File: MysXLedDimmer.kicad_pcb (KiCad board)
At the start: 2 copper layers, 18.5 x 26.1 mm, 8 parts, among them P1 MYSX_1.3, P2 CONN_01X02, P3 CONN_01X02, P4 CONN_01X02, Q1 IRLZ44N, Q2 IRLZ44N

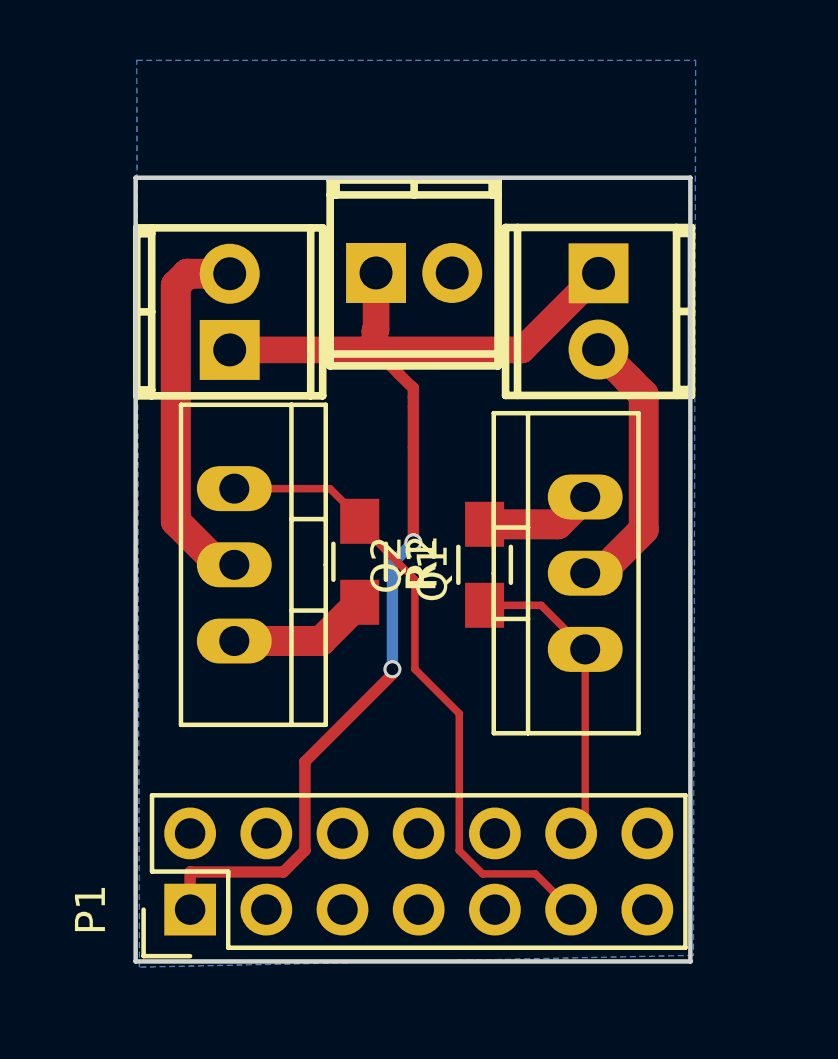
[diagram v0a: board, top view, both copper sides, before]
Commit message: Changed to use IRLML2502 in sot23
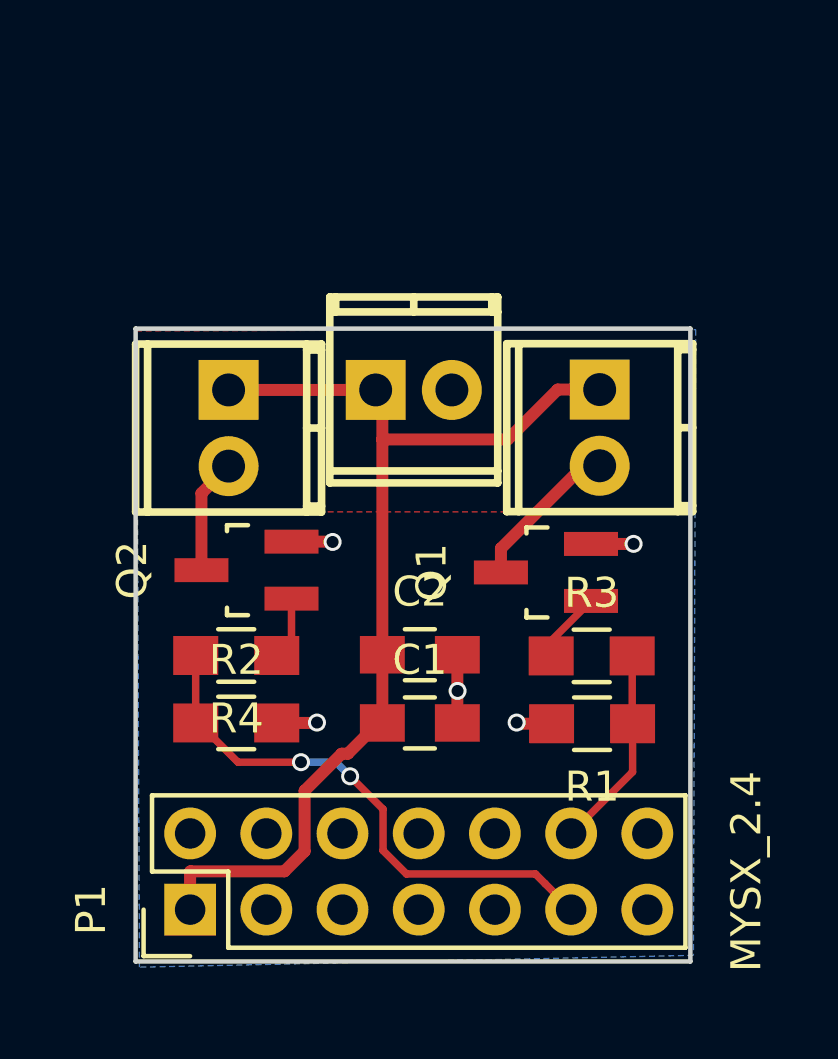
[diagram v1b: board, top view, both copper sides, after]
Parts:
- added C1: C, Capacitors_SMD:C_0805_HandSoldering, F.Cu at (145.5, 118.0)
- added C2: CP, Capacitors_SMD:C_0805_HandSoldering, F.Cu at (145.5, 115.7)
- added R3: 27, Resistors_SMD:R_0805_HandSoldering, F.Cu at (151.2, 115.7)
- added R4: 27, Resistors_SMD:R_0805_HandSoldering, F.Cu at (139.4, 115.7)
- P1: value MYSX_1.3 -> MYSX_2.4; footprint mysensors_connectors:MYSX_1.3 -> mysensors_connectors:MYSX_2.3
- Q1, Q2: value IRLZ44N -> IRLML2502; footprint TO_SOT_Packages_THT:TO-220_Neutral123_Vertical -> TO_SOT_Packages_SMD:SOT-23_Handsoldering
- R1, R2: value 2k2 -> 100k
- moved R2 6.77 mm to (139.4, 118.0), turned to 0 degrees
- moved R1 6.39 mm to (151.2, 118.0), turned to 180 degrees
- moved P2 3.90 mm to (145.3, 106.9)
- moved P4 3.87 mm to (139.1, 108.1), turned to 90 degrees
- moved P3 3.87 mm to (151.5, 108.1)
- moved Q1 1.31 mm to (149.7, 113.0)
- moved Q2 0.44 mm to (139.7, 112.9), turned to 90 degrees
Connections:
- Q1 pad 1: Net-(P1-Pad12) -> Net-(Q1-Pad1)
- Q1 pad 2: Net-(P3-Pad2) -> GND
- Q1 pad 3: GND -> Net-(P3-Pad2)
- Q2 pad 1: Net-(P1-Pad11) -> Net-(Q2-Pad1)
- Q2 pad 2: Net-(P4-Pad2) -> GND
- Q2 pad 3: GND -> Net-(P4-Pad2)
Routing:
- net Net-(P4-Pad2): track 12.4 -> 3.84 mm
- net +12V: track 40.0 -> 34.9 mm, vias 2 -> 0
- net Net-(P3-Pad2): track 9.18 -> 5.23 mm
- net Net-(P1-Pad11): track 22.1 -> 18.1 mm, vias 0 -> 2
- net Net-(P1-Pad12): track 10.3 -> 7.44 mm
- net Net-(Q1-Pad1): track 0.00 -> 2.38 mm
- net Net-(Q2-Pad1): track 0.00 -> 2.20 mm
- net GND: track 8.44 -> 7.60 mm, vias 0 -> 5
- added copper zone on F.Cu, net +12V
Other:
- board size 18.5 x 26.1 mm -> 18.5 x 21.1 mm
- net class Power: trace_width 0.381 -> 0.4
